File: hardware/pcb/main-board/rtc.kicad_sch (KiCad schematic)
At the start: 11 parts, among them U801 PCF85063AT/AAZ RTC, U803 74LVC1G07, Y801 ECS-.327-9-34B-C-TR

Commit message: start next board iteration, add latch and pico power bits
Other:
- note added: "5V supply comes from the power module. It's switched on permanently."
- note removed: "5V supply comes from the power module. It's switched on when the double shift keys are pressed."
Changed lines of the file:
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@@
 	(title_block
 		(title "Z88R - Z88 Recreated")
-		(date "2024-08-23")
-		(rev "20240823")
+		(date "2025-12-19")
+		(rev "20251219WIP")
 		(company "Fountain and Menadue")
 	)
@@
 		)
 	)
-	(text "5V supply comes from\nthe power module. It's\nswitched on when the\ndouble shift keys are\npressed."
+	(text "5V supply comes from\nthe power module. It's\nswitched on permanently."
 		(exclude_from_sim no)
-		(at 26.924 18.796 0)
-		(effects
-			(font
-				(size 1.27 1.27)
+		(at 21.59 19.05 0)
+		(effects
+			(font
+				(size 1 1)
 			)
 			(justify left)
@@
 	(label "RTC_PWR"
 		(at 68.58 35.56 0)
-		(fields_autoplaced yes)
 		(effects
 			(font
@@
 	(label "CELL_PWR"
 		(at 30.48 48.26 180)
-		(fields_autoplaced yes)
 		(effects
 			(font
@@
 	(label "RTC_PWR"
 		(at 148.59 38.1 0)
-		(fields_autoplaced yes)
 		(effects
 			(font
@@
 		(shape output)
 		(at 248.92 50.8 0)
-		(fields_autoplaced yes)
-		(effects
-			(font
+		(effects
+			(font

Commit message: add i2c connection to the support pico so it can control the RTC
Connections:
- net CM4_I2C_CLK renamed MAIN_I2C_CLK
- net CM4_I2C_DAT renamed MAIN_I2C_DAT
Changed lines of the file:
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@@
 		)
 	)
-	(global_label "CM4_I2C_CLK"
+	(global_label "MAIN_I2C_CLK"
 		(shape input)
 		(at 116.84 40.64 0)
@@
 		)
 		(property "Intersheetrefs" "${INTERSHEET_REFS}"
-			(at 131.6895 40.64 0)
+			(at 132.2339 40.64 0)
 			(effects
 				(font
@@
 		)
 	)
-	(global_label "CM4_I2C_DAT"
+	(global_label "MAIN_I2C_DAT"
 		(shape input)
 		(at 116.84 43.18 0)
@@
 		)
 		(property "Intersheetrefs" "${INTERSHEET_REFS}"
-			(at 131.4476 43.18 0)
+			(at 131.992 43.18 0)
 			(effects
 				(font

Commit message: make a start on RP2040 to replace the KB pico
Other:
- title: Z88R - Z88 Recreated -> Z88R - Z88 Recreation
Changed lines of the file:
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@@
 	(paper "A4")
 	(title_block
-		(title "Z88R - Z88 Recreated")
-		(date "2025-12-19")
-		(rev "20251219WIP")
+		(title "Z88R - Z88 Recreation")
+		(date "2025-12-30")
+		(rev "20251230WIP")
 		(company "Fountain and Menadue")
 	)

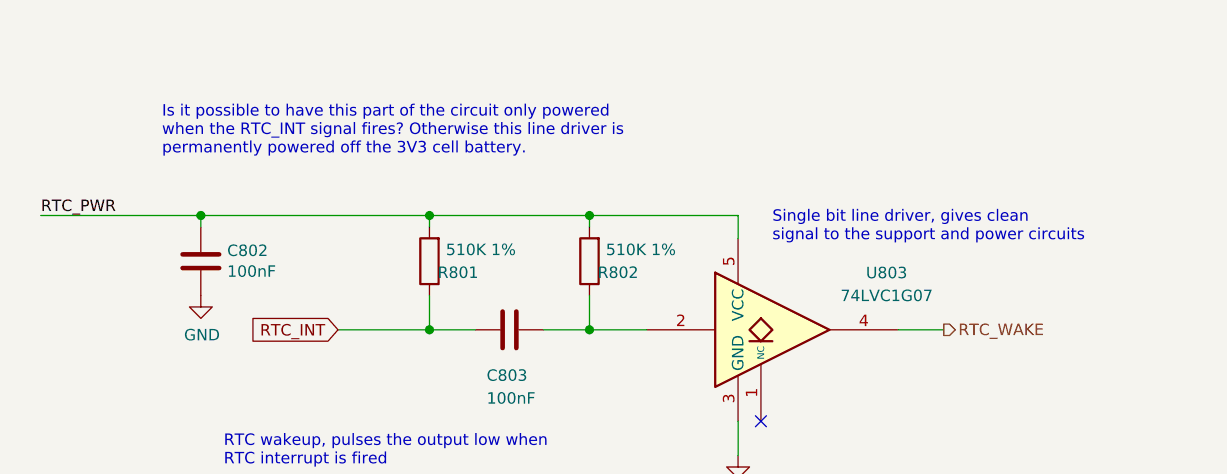
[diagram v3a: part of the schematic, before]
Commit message: more working out of the KB pico replacement
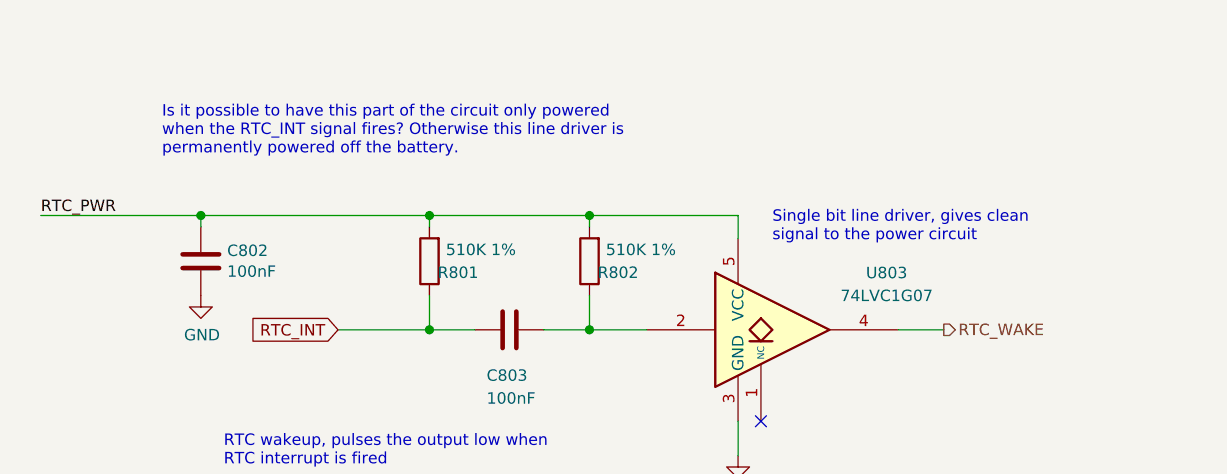
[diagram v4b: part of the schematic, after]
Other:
- note added: "Is it possible to have this part of the circuit only powered when the RTC_INT signal fires? Otherwise this line driver is permanently powered off the battery."
- note added: "Single bit line driver, gives clean signal to the power circuit"
- note removed: "Is it possible to have this part of the circuit only powered when the RTC_INT signal fires? Otherwise this line driver is permanently powered off the 3V3 cell battery."
- note removed: "Single bit line driver, gives clean signal to the support and power circuits"
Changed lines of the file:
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@@
 		)
 	)
-	(text "Single bit line driver, gives clean\nsignal to the support and power circuits"
+	(text "Single bit line driver, gives clean\nsignal to the power circuit"
 		(exclude_from_sim no)
 		(at 229.87 39.37 0)
@@
 		)
 	)
-	(text "Is it possible to have this part of the circuit only powered\nwhen the RTC_INT signal fires? Otherwise this line driver is\npermanently powered off the 3V3 cell battery."
+	(text "Is it possible to have this part of the circuit only powered\nwhen the RTC_INT signal fires? Otherwise this line driver is\npermanently powered off the battery."
 		(exclude_from_sim no)
 		(at 162.052 28.702 0)
